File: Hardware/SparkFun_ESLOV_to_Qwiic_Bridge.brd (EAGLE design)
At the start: 22.9 x 8.9 mm, 17 parts, among them J2 QWIIC_RA, U1 3.3V

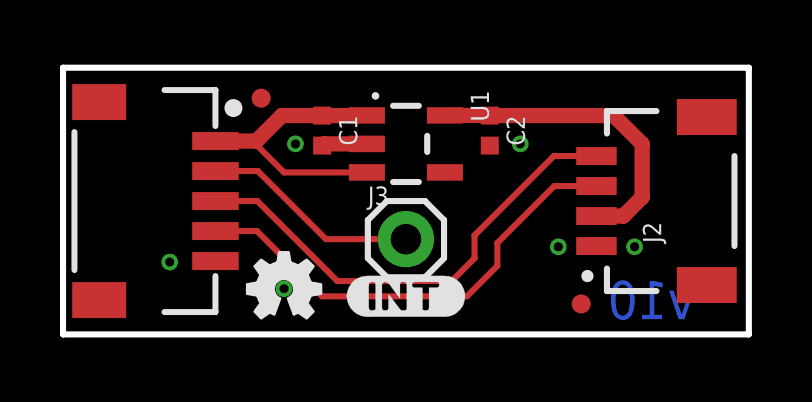
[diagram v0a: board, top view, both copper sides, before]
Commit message: Rename Board File
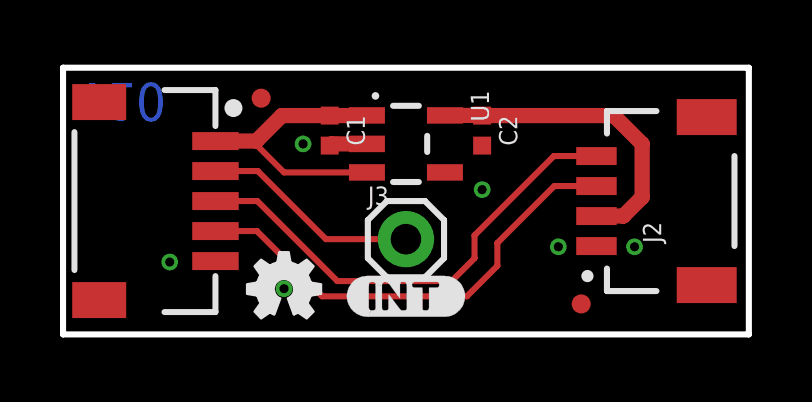
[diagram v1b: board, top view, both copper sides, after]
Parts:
- J1: value (none) -> ESLOV RA
- U$4: device output:ADAPTER0 -> output:ESLOV_TO_QWIIC_BRIDGE0
- moved LOGO1 1.78 mm to (11.4, 6.60), turned to 180 degrees
- moved C1 0.25 mm to (8.89, 6.79)
- moved U$4 0.25 mm to (11.4, 1.02), turned to 180 degrees
- moved C2 0.25 mm to (14.0, 6.79)
- turned U$2 to 270 degrees
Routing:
- net 5V: track 9.65 -> 10.9 mm
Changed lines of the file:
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@@
 <layer number="37" name="tTest" color="7" fill="1" visible="no" active="yes"/>
 <layer number="38" name="bTest" color="7" fill="1" visible="no" active="yes"/>
-<layer number="39" name="tKeepout" color="4" fill="11" visible="no" active="yes"/>
-<layer number="40" name="bKeepout" color="1" fill="11" visible="no" active="yes"/>
-<layer number="41" name="tRestrict" color="4" fill="10" visible="no" active="yes"/>
-<layer number="42" name="bRestrict" color="1" fill="10" visible="no" active="yes"/>
-<layer number="43" name="vRestrict" color="2" fill="10" visible="no" active="yes"/>
+<layer number="39" name="tKeepout" color="4" fill="11" visible="yes" active="yes"/>
+<layer number="40" name="bKeepout" color="1" fill="11" visible="yes" active="yes"/>
+<layer number="41" name="tRestrict" color="4" fill="10" visible="yes" active="yes"/>
+<layer number="42" name="bRestrict" color="1" fill="10" visible="yes" active="yes"/>
+<layer number="43" name="vRestrict" color="2" fill="10" visible="yes" active="yes"/>
 <layer number="44" name="Drills" color="7" fill="1" visible="no" active="yes"/>
 <layer number="45" name="Holes" color="7" fill="1" visible="yes" active="yes"/>
@@
 <wire x1="22.86" y1="8.89" x2="0" y2="8.89" width="0.2032" layer="20"/>
 <wire x1="0" y1="8.89" x2="0" y2="0" width="0.2032" layer="20"/>
-<text x="21.082" y="0.508" size="1.27" layer="16" font="vector" ratio="15" rot="MR0">v10</text>
+<text x="0.508" y="8.382" size="1.27" layer="16" font="vector" ratio="15" rot="SMR180">v10</text>
 <dimension x1="0" y1="0" x2="11.43" y2="3.175" x3="-0.762" y3="1.5875" textsize="1.27" textratio="15" layer="47" dtype="vertical" unit="inch" precision="3"/>
 <dimension x1="0" y1="0" x2="5.08" y2="4.445" x3="-3.048" y3="2.2225" textsize="1.27" textratio="15" layer="47" dtype="vertical" unit="inch" precision="3"/>
@@
 </autorouter>
 <elements>
-<element name="C1" library="SparkFun-Capacitors" package="0402-TIGHT" value="1.0uF" x="8.636" y="6.7945" smashed="yes" rot="R270">
-<attribute name="NAME" x="9.198" y="6.7945" size="0.6096" layer="25" font="vector" ratio="20" rot="R270" align="bottom-center"/>
-<attribute name="PROD_ID" value="CAP-12417" x="-2.794" y="-31.3055" size="1.778" layer="27" rot="R270" display="off"/>
-<attribute name="VALUE" x="8.074" y="6.7945" size="0.6096" layer="27" font="vector" ratio="20" rot="R270" align="top-center"/>
-</element>
-<element name="C2" library="SparkFun-Capacitors" package="0402-TIGHT" value="1.0uF" x="14.224" y="6.7945" smashed="yes" rot="R270">
-<attribute name="NAME" x="14.786" y="6.7945" size="0.6096" layer="25" font="vector" ratio="20" rot="R270" align="bottom-center"/>
-<attribute name="PROD_ID" value="CAP-12417" x="2.794" y="-35.1155" size="1.778" layer="27" rot="R270" display="off"/>
-<attribute name="VALUE" x="13.662" y="6.7945" size="0.6096" layer="27" font="vector" ratio="20" rot="R270" align="top-center"/>
+<element name="C1" library="SparkFun-Capacitors" package="0402-TIGHT" value="1.0uF" x="8.89" y="6.7945" smashed="yes" rot="R270">
+<attribute name="NAME" x="9.452" y="6.7945" size="0.6096" layer="25" font="vector" ratio="20" rot="R270" align="bottom-center"/>
+<attribute name="PROD_ID" value="CAP-12417" x="-2.54" y="-31.3055" size="1.778" layer="27" rot="R270" display="off"/>
+<attribute name="VALUE" x="8.328" y="6.7945" size="0.6096" layer="27" font="vector" ratio="20" rot="R270" align="top-center"/>
+</element>
+<element name="C2" library="SparkFun-Capacitors" package="0402-TIGHT" value="1.0uF" x="13.97" y="6.7945" smashed="yes" rot="R270">
+<attribute name="NAME" x="14.532" y="6.7945" size="0.6096" layer="25" font="vector" ratio="20" rot="R270" align="bottom-center"/>
+<attribute name="PROD_ID" value="CAP-12417" x="2.54" y="-35.1155" size="1.778" layer="27" rot="R270" display="off"/>
+<attribute name="VALUE" x="13.408" y="6.7945" size="0.6096" layer="27" font="vector" ratio="20" rot="R270" align="top-center"/>
 </element>
 <element name="FRAME1" library="SparkFun-Aesthetics" package="CREATIVE_COMMONS" value="FRAME-LETTER" x="-7.62" y="-12.446" smashed="yes">
@@
 <attribute name="REV" value="v10" x="72.39" y="-13.716" size="1.778" layer="27" display="off"/>
 </element>
-<element name="J1" library="ESLOV" package="JST_5_1MM_RA" value="" x="5.08" y="4.445" smashed="yes" rot="R270"/>
+<element name="J1" library="ESLOV" package="JST_5_1MM_RA" value="ESLOV RA" x="5.08" y="4.445" smashed="yes" rot="R270">
+<attribute name="PN" value="SM05B-SRSS-TB" x="5.08" y="4.445" size="1.778" layer="27" rot="R270" display="off"/>
+<attribute name="PROD_ID" value="CONN-20121" x="5.08" y="4.445" size="1.778" layer="27" rot="R270" display="off"/>
+<attribute name="VALUE" value="ESLOV RA" x="5.08" y="4.445" size="1.778" layer="27" rot="R270" display="off"/>
+</element>
 <element name="J2" library="SparkFun-Connectors" package="JST04_1MM_RA" value="QWIIC_RA" x="17.78" y="4.445" smashed="yes" rot="R90">
 <attribute name="NAME" x="19.939" y="3.048" size="0.6096" layer="25" font="vector" ratio="20" rot="R90"/>
@@
 </element>
 <element name="U$1" library="output" package="#INT#0" value="" x="11.43" y="1.27" smashed="yes"/>
-<element name="LOGO1" library="SparkFun-Aesthetics" package="SFE_LOGO_NAME_FLAME_.1" value="SFE_LOGO_NAME_FLAME.1_INCH" x="11.43" y="4.826" smashed="yes" rot="MR0"/>
+<element name="LOGO1" library="SparkFun-Aesthetics" package="SFE_LOGO_NAME_FLAME_.1" value="SFE_LOGO_NAME_FLAME.1_INCH" x="11.43" y="6.604" smashed="yes" rot="MR180"/>
 <element name="LOGO2" library="SparkFun-Aesthetics" package="OSHW-LOGO-MINI" value="OSHW-LOGOMINI" x="7.366" y="1.524" smashed="yes"/>
 <element name="LOGO3" library="SparkFun-Aesthetics" package="QWIIC_5.5MM" value="QWIIC_LOGO_CONNECTOR" x="21.59" y="4.445" smashed="yes" rot="MR270"/>
 <element name="U$3" library="SparkFun-Aesthetics" package="SFE_LOGO_FLAME_STOP_.1" value="" x="15.621" y="1.778" smashed="yes"/>
-<element name="U$2" library="output" package="ESLOV0" value="" x="0.889" y="4.445" smashed="yes" rot="MR90"/>
-<element name="U$4" library="output" package="ADAPTER0" value="" x="11.43" y="1.27" smashed="yes" rot="MR0"/>
+<element name="U$2" library="output" package="ESLOV0" value="" x="0.889" y="4.445" smashed="yes" rot="MR270"/>
 <element name="FD1" library="SparkFun-Aesthetics" package="FIDUCIAL-MICRO" value="FIDUCIALUFIDUCIAL" x="17.272" y="1.016" smashed="yes"/>
 <element name="FD2" library="SparkFun-Aesthetics" package="FIDUCIAL-MICRO" value="FIDUCIALUFIDUCIAL" x="6.604" y="7.874" smashed="yes"/>
 <element name="U$5" library="SparkFun-Aesthetics" package="ORDERING_INSTRUCTIONS" value="" x="29.718" y="49.784" smashed="yes"/>
+<element name="U$4" library="output" package="ESLOV_TO_QWIIC_BRIDGE0" value="" x="11.43" y="1.016" smashed="yes" rot="MR180"/>
 </elements>
 <signals>
@@
 <contactref element="U1" pad="2"/>
 <contactref element="C2" pad="2"/>
-<wire x1="8.636" y1="6.2945" x2="8.6915" y2="6.35" width="0.508" layer="1"/>
-<wire x1="8.6915" y1="6.35" x2="10.1299" y2="6.35" width="0.508" layer="1"/>
+<wire x1="8.89" y1="6.2945" x2="8.9455" y2="6.35" width="0.508" layer="1"/>
+<wire x1="8.9455" y1="6.35" x2="10.1299" y2="6.35" width="0.508" layer="1"/>
 <polygon width="0.2032" layer="1" isolate="0.3048">
 <vertex x="0" y="8.89"/>
@@
 <via x="7.366" y="1.524" extent="1-16" drill="0.3048"/>
 <via x="16.51" y="2.921" extent="1-16" drill="0.3048"/>
-<via x="7.747" y="6.35" extent="1-16" drill="0.3048"/>
-<via x="15.24" y="6.35" extent="1-16" drill="0.3048"/>
+<via x="8.001" y="6.35" extent="1-16" drill="0.3048"/>
+<via x="13.97" y="4.826" extent="1-16" drill="0.3048"/>
 <via x="19.05" y="2.921" extent="1-16" drill="0.3048"/>
 <via x="3.556" y="2.413" extent="1-16" drill="0.3048"/>
@@
 <contactref element="U1" pad="5"/>
 <contactref element="J2" pad="2"/>
-<wire x1="12.7301" y1="7.3" x2="14.2185" y2="7.3" width="0.508" layer="1"/>
-<wire x1="14.2185" y1="7.3" x2="14.224" y2="7.2945" width="0.508" layer="1"/>
-<wire x1="14.224" y1="7.2945" x2="18.3595" y2="7.2945" width="0.508" layer="1"/>
+<wire x1="12.7301" y1="7.3" x2="13.9645" y2="7.3" width="0.508" layer="1"/>
+<wire x1="13.9645" y1="7.3" x2="13.97" y2="7.2945" width="0.508" layer="1"/>
+<wire x1="13.97" y1="7.2945" x2="18.3595" y2="7.2945" width="0.508" layer="1"/>
 <wire x1="18.677" y1="3.945" x2="17.78" y2="3.945" width="0.508" layer="1"/>
 <wire x1="18.3595" y1="7.2945" x2="19.304" y2="6.35" width="0.508" layer="1"/>
@@
 <contactref element="C1" pad="1"/>
 <wire x1="5.08" y1="6.445" x2="6.445" y2="6.445" width="0.508" layer="1"/>
-<wire x1="7.2945" y1="7.2945" x2="8.636" y2="7.2945" width="0.508" layer="1"/>
+<wire x1="7.2945" y1="7.2945" x2="8.89" y2="7.2945" width="0.508" layer="1"/>
 <wire x1="6.445" y1="6.445" x2="7.2945" y2="7.2945" width="0.508" layer="1"/>
-<wire x1="8.636" y1="7.2945" x2="10.1244" y2="7.2945" width="0.508" layer="1"/>
+<wire x1="8.89" y1="7.2945" x2="10.1244" y2="7.2945" width="0.508" layer="1"/>
 <wire x1="10.1244" y1="7.2945" x2="10.1299" y2="7.3" width="0.508" layer="1"/>
 <wire x1="10.1299" y1="5.4" x2="7.363" y2="5.4" width="0.2032" layer="1"/>
 <wire x1="7.363" y1="5.4" x2="6.318" y2="6.445" width="0.2032" layer="1"/>
-<wire x1="6.318" y1="6.445" x2="5.08" y2="6.445" width="0" layer="19" extent="1-1"/>
+<wire x1="6.318" y1="6.445" x2="5.08" y2="6.445" width="0.2032" layer="1"/>
 </signal>
 </signals>
